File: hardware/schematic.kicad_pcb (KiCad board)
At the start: 2 copper layers, 169.7 x 127.8 mm, 118 parts, among them J3 USB_C_Receptacle_USB2.0_16P

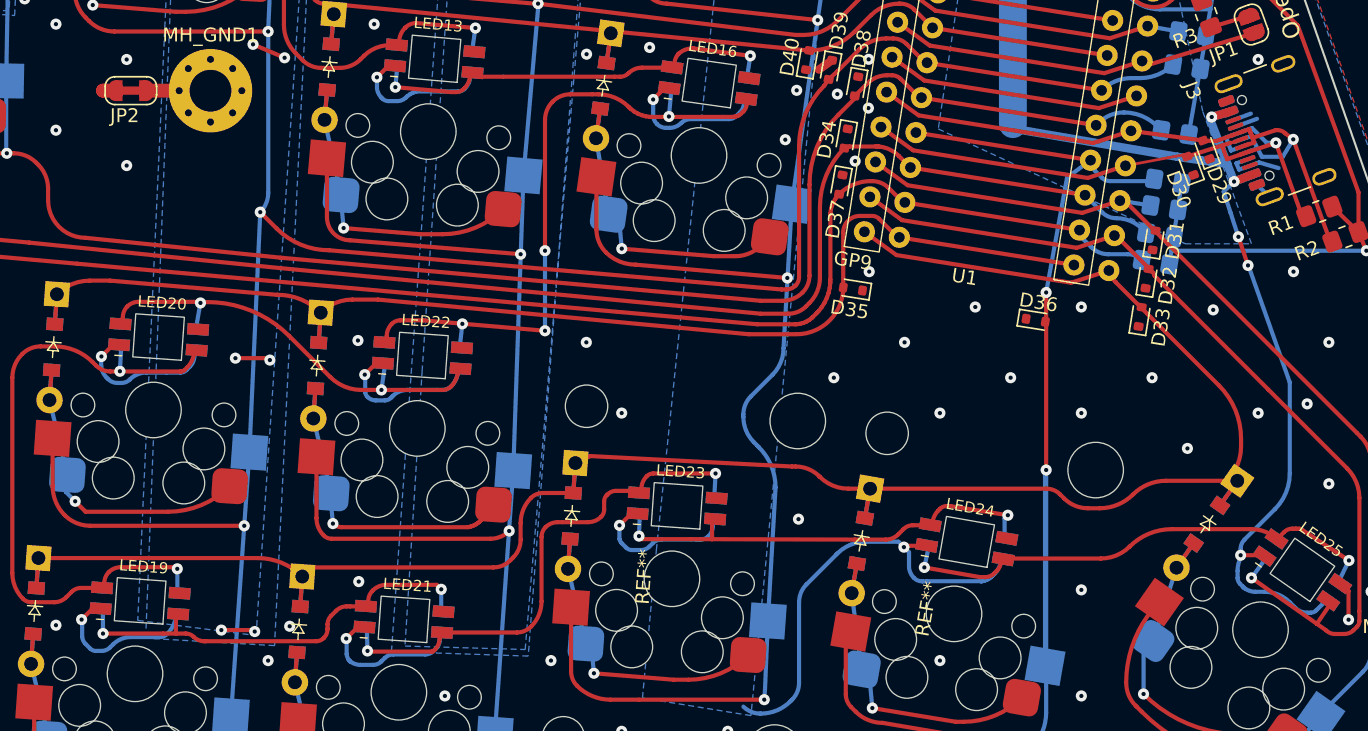
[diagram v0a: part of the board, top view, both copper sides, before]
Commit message: Fix disconnected pours
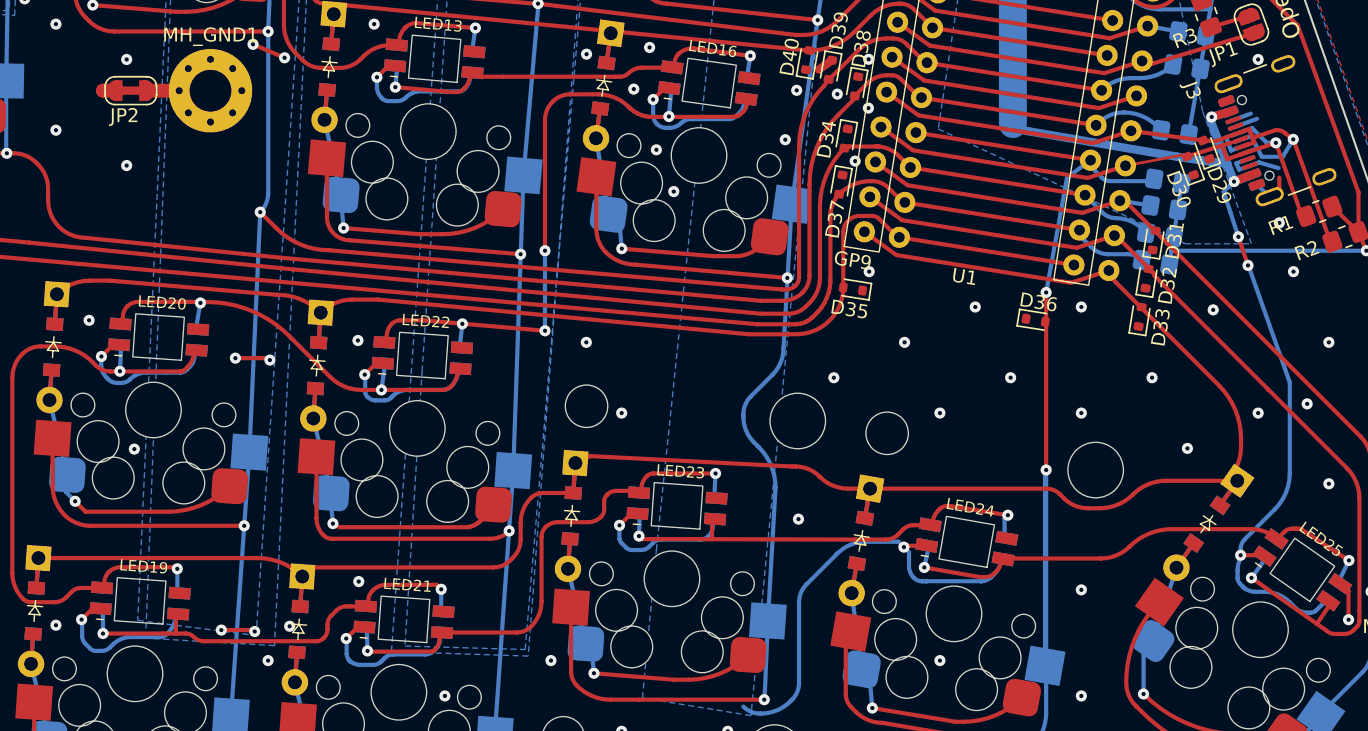
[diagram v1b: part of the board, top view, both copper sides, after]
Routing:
- net GND: track 28.6 -> 30.3 mm, vias 163 -> 169

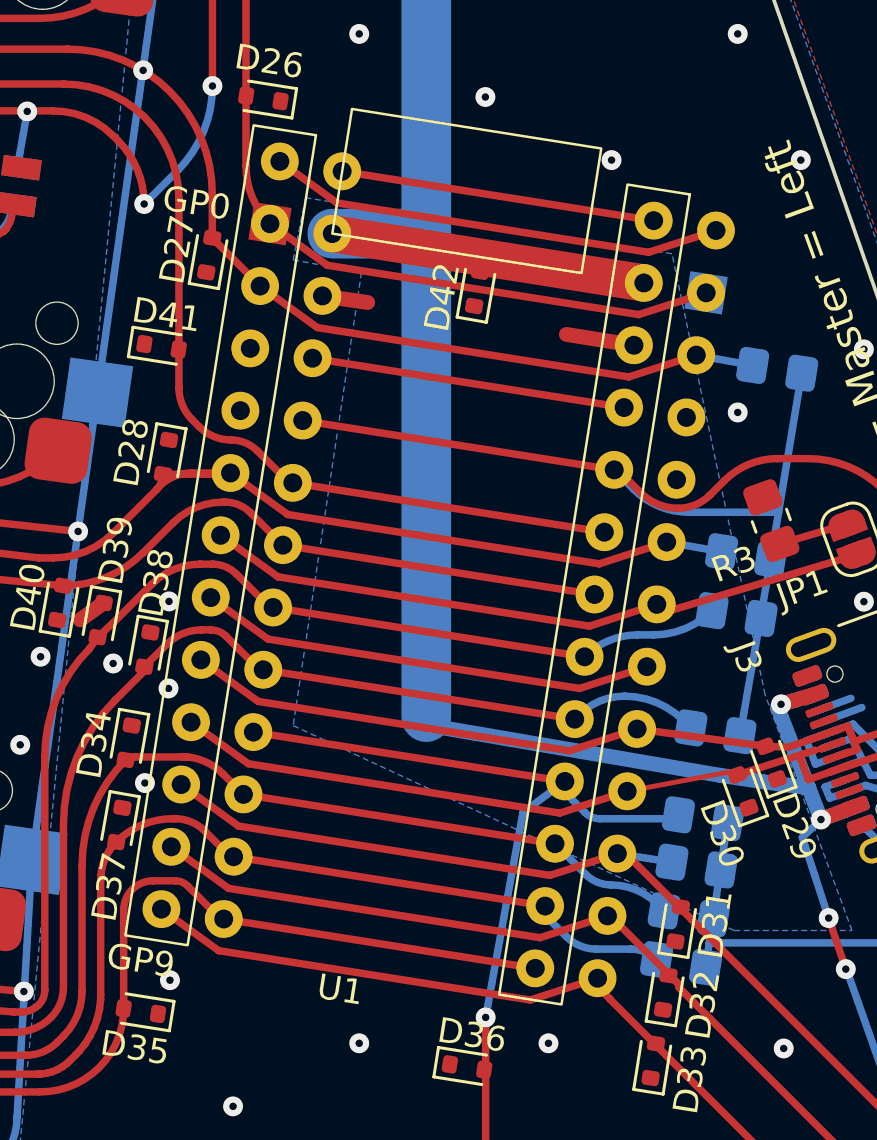
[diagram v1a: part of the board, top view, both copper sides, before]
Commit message: Widen MCU header holes slightly
The holes were a big snug, widen from 0.7mm -> 1.0mm.
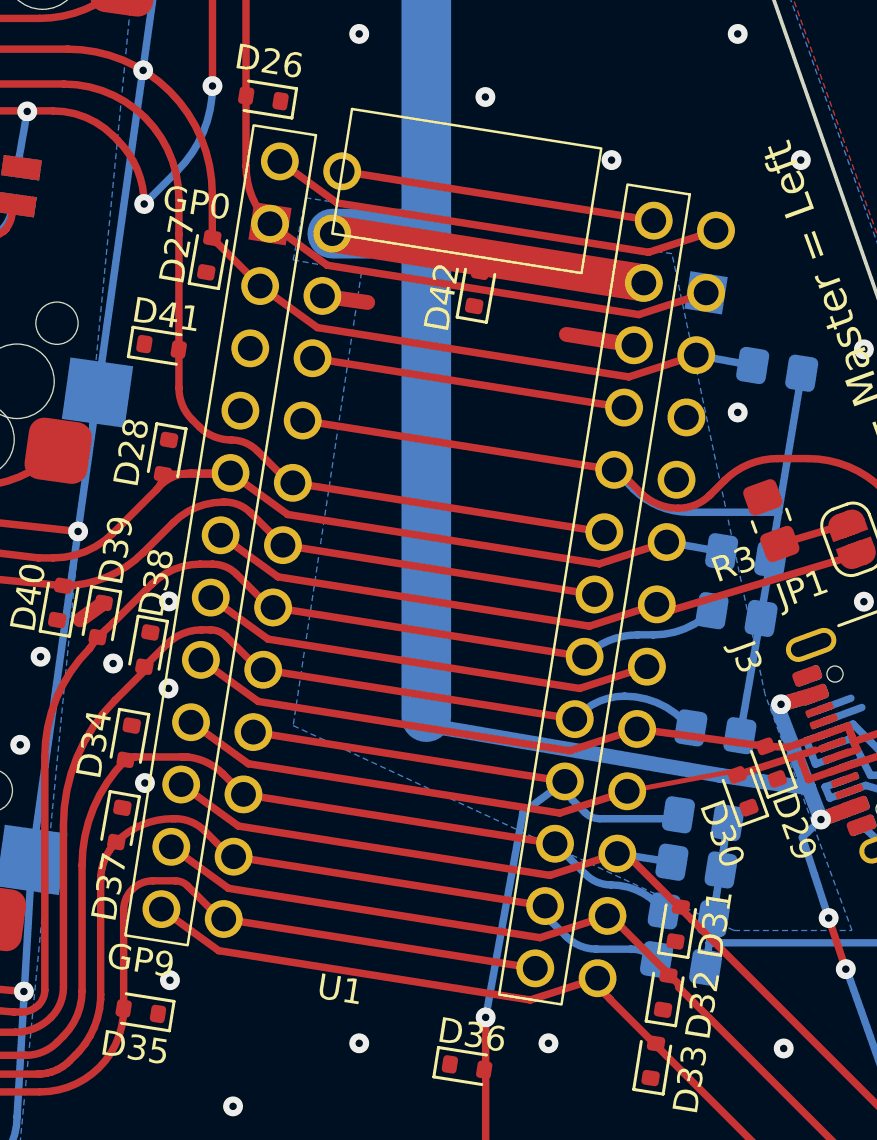
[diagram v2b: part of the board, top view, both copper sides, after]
